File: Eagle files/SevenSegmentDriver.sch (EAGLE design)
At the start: 12 parts, among them IC1 74HC595D

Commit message: Ready for Fabbing
Silk Screens added and last minute DRC checks done.
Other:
- note added: "1.0"
- note added: "Alan Fernandez"
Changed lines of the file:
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@@
 <part name="RCLK" library="wirepad" deviceset="WIREPAD" device="1,6/0,9" value="WIREPAD1,6/0,9"/>
 <part name="GND" library="wirepad" deviceset="WIREPAD" device="1,6/0,9" value="WIREPAD1,6/0,9"/>
+<part name="FRAME1" library="frames" deviceset="LETTER_L" device=""/>
 </parts>
 <sheets>
 <sheet>
 <plain>
+<text x="114.3" y="-25.4" size="5.08" layer="94">Alan Fernandez</text>
+<text x="198.12" y="-45.72" size="5.08" layer="94">1.0</text>
 </plain>
 <instances>
@@
 <instance part="GND" gate="G$1" x="10.16" y="12.7"/>
 <instance part="IC1" gate="P" x="83.82" y="50.8" rot="R90"/>
+<instance part="FRAME1" gate="G$1" x="-38.1" y="-50.8"/>
+<instance part="FRAME1" gate="G$2" x="109.22" y="-50.8"/>
 </instances>
 <busses>

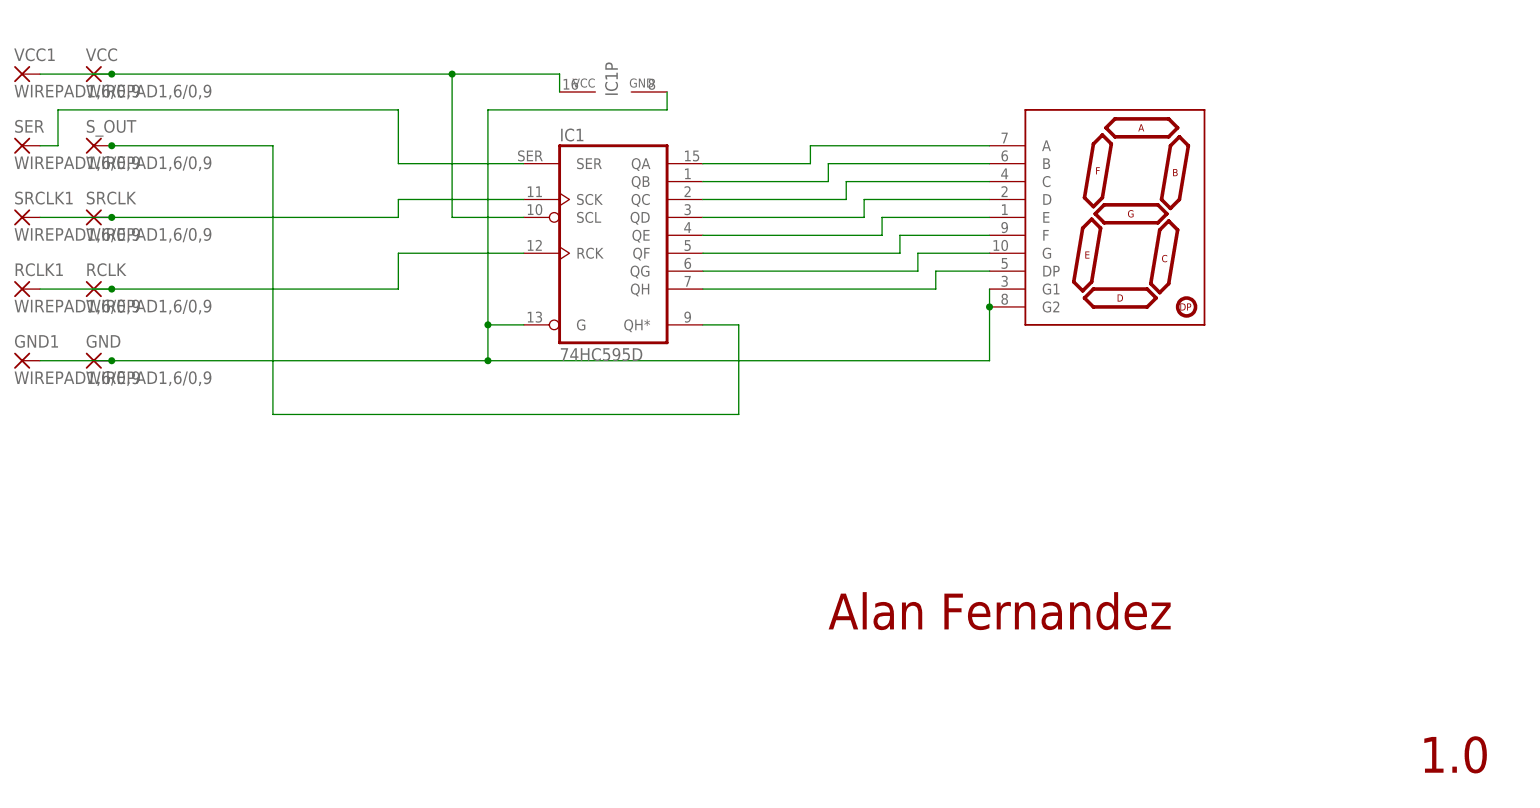
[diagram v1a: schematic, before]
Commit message: aaaaaaaaaaaaaaaaaaaaaaaaaaaaaaaaaaaa
Cleaned up schematics, replaced wire solder points with header pin
mounts for standardization, recreated a broken file and dealt with the
confusion and insanity that followed.
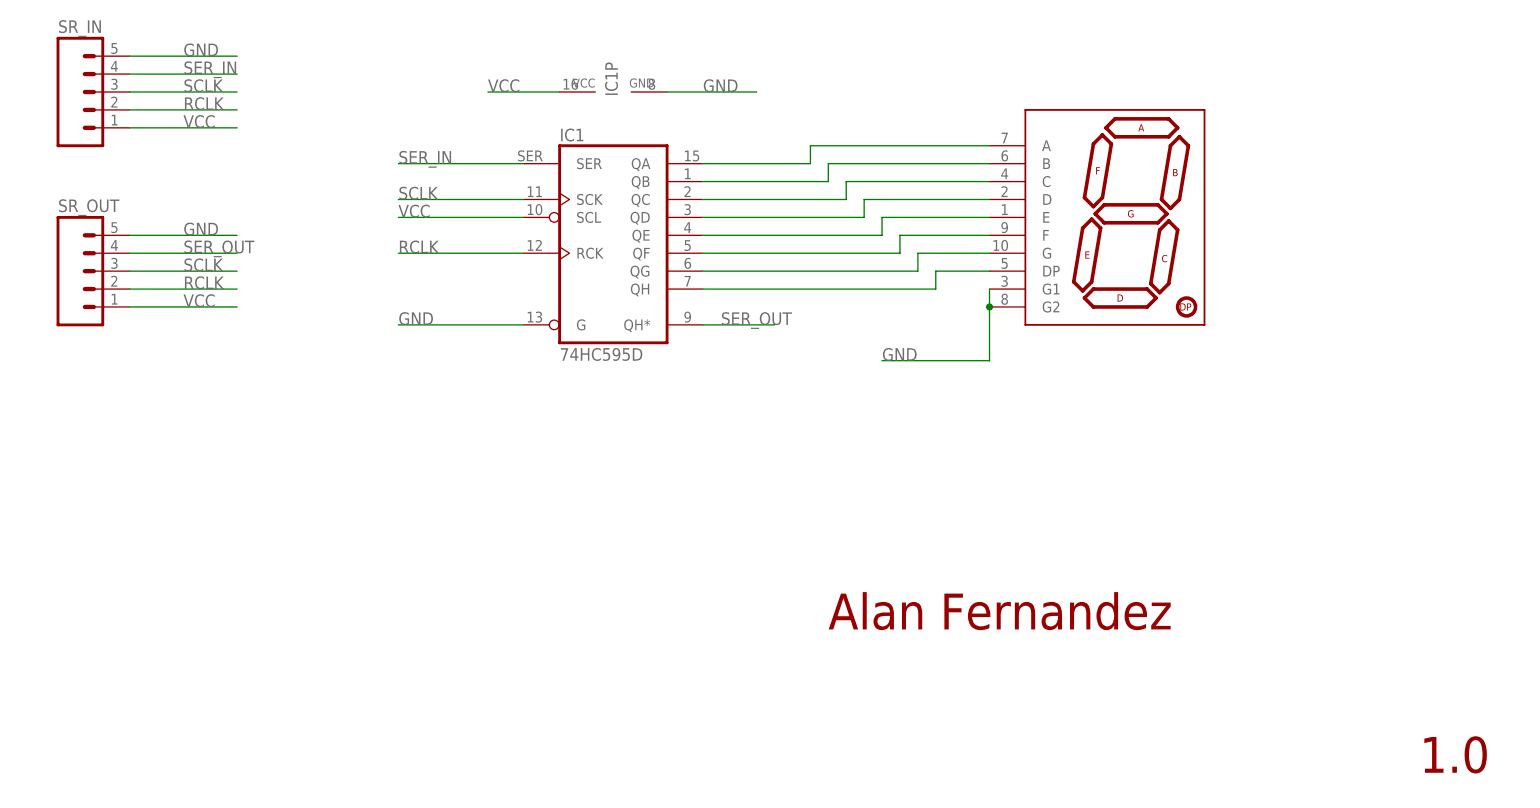
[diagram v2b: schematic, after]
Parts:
- removed GND, GND1, RCLK, RCLK1, SER, SRCLK, SRCLK1, S_OUT: WIREPAD1,6/0,9, wirepad:WIREPAD1,6/0,9
- removed VCC, VCC1: WIREPAD1,6/0,9, smallestWirepadSquare:WIREPAD1,6/0,9
- added SR_IN, SR_OUT: (no value), SparkFun-Connectors:M05PTH
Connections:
- removed net N$11: IC1A.QH*, S_OUT.P
- removed net N$12: IC1A.RCK, RCLK.P, RCLK1.P
- removed net N$13: IC1A.SCK, SRCLK.P, SRCLK1.P
- removed net N$14: IC1A.SER, SER.P
- new net RCLK: IC1A.RCK, SR_IN.2, SR_OUT.2
- new net SCLK: IC1A.SCK, SR_IN.3, SR_OUT.3
- new net SER_IN: IC1A.SER, SR_IN.4
- new net SER_OUT: IC1A.QH*, SR_OUT.4
- net GND: now also SR_IN.5, SR_OUT.5; no longer GND.P, GND1.P
- net VCC: now also SR_IN.1, SR_OUT.1; no longer VCC.P, VCC1.P
